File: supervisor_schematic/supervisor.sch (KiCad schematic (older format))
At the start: 13 parts

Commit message: supervisor almost done
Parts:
- added 10K: R6, symbol Device:R
- added C?: C1, symbol pspice:C
- added LS?: PS1240P02BT, PS1240P02BT, symbol Noggin:PS1240P02BT
- added R5: 1K, symbol Device:R
- added SW?: SW_Push, symbol Switch:SW_Push
- added U?: OLED-1602A, symbol Noggin:OLED-1602A
- D1: renamed from D?; value LED -> Green LED
- D2: renamed from D?; value LED -> Red LED
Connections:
- net +3V3: now also 10K.1, U?.~ (VSS)
- net GND: now also C?.2, LS?.2, U?.~ (VSS)
- net CS: now reaches ANT?.19 (CMD)
- net CS: now also U?.~ (VSS)
- net CLK: now reaches ANT?.20 (CLK)
- net CLK: now also U?.~ (VSS)
- net SD0: now reaches ANT?.21 (SD0)
- net SD0: now also U?.~ (VSS)
- net SD1: now reaches ANT?.22 (SD1)
- net SD1: now also U?.~ (VSS)
- net at ANT?.23 (IO15): now also R5.2
- net at ANT?.3 (EN): now also 10K.2, C?.1, SW?.1
- new net: LS?.1, R5.1
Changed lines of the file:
@@
 	4700 3000 4450 3000
 $Comp
-L Device:LED D?
+L Device:LED D1
 U 1 1 62152961
 P 4450 3400
-F 0 "D?" H 4443 3616 50  0000 C CNN
-F 1 "LED" H 4443 3525 50  0000 C CNN
+F 0 "D1" H 4443 3616 50  0000 C CNN
+F 1 "Green LED" H 4443 3525 50  0000 C CNN
 F 2 "" H 4450 3400 50  0001 C CNN
 F 3 "~" H 4450 3400 50  0001 C CNN
@@
 $EndComp
 $Comp
-L Device:LED D?
+L Device:LED D2
 U 1 1 62153081
 P 4000 3500
-F 0 "D?" H 3993 3716 50  0000 C CNN
-F 1 "LED" H 3993 3625 50  0000 C CNN
+F 0 "D2" H 3993 3716 50  0000 C CNN
+F 1 "Red LED" H 3993 3625 50  0000 C CNN
 F 2 "" H 4000 3500 50  0001 C CNN
 F 3 "~" H 4000 3500 50  0001 C CNN
@@
 Wire Wire Line
 	6450 5400 6300 5400
-Wire Wire Line
-	6450 5400 6600 5400
 Connection ~ 6450 5400
 $Comp
@@
 	1    0    0    -1
 $EndComp
+$Comp
+L Noggin:PS1240P02BT LS?
+U 1 1 6215B3F6
+P 6950 3100
+F 0 "LS?" H 7578 3096 50  0000 L CNN
+F 1 "PS1240P02BT" H 7578 3005 50  0000 L CNN
+F 2 "PS1240P02BT" H 7600 3200 50  0001 L CNN
+F 3 "https://product.tdk.com/system/files/dam/doc/product/sw_piezo/sw_piezo/piezo-buzzer/catalog/piezoelectronic_buzzer_ps_en.pdf" H 7600 3100 50  0001 L CNN
+F 4 "Piezoelectric Buzzers, Sound Pressure Level=70dB min, Freq.=4000Hz nom" H 7600 3000 50  0001 L CNN "Description"
+F 5 "TDK" H 7600 2800 50  0001 L CNN "Manufacturer_Name"
+F 6 "PS1240P02BT" H 7600 2700 50  0001 L CNN "Manufacturer_Part_Number"
+F 7 "810-PS1240P02BT" H 7600 2600 50  0001 L CNN "Mouser Part Number"
+F 8 "https://www.mouser.co.uk/ProductDetail/TDK/PS1240P02BT?qs=d7g9p1yFhWaZXSY9MjKMkw%3D%3D" H 7600 2500 50  0001 L CNN "Mouser Price/Stock"
+F 9 "PS1240P02BT" H 7600 2400 50  0001 L CNN "Arrow Part Number"
+F 10 "https://www.arrow.com/en/products/ps1240p02bt/tdk?region=nac" H 7600 2300 50  0001 L CNN "Arrow Price/Stock"
+	1    6950 3100
+	1    0    0    -1
+$EndComp
+$Comp
+L Device:R R5
+U 1 1 6215ED9A
+P 6500 3100
+F 0 "R5" V 6293 3100 50  0000 C CNN
+F 1 "1K" V 6384 3100 50  0000 C CNN
+F 2 "" V 6430 3100 50  0001 C CNN
+F 3 "~" H 6500 3100 50  0001 C CNN
+	1    6500 3100
+	0    1    1    0
+$EndComp
+Wire Wire Line
+	6100 3100 6350 3100
+Wire Wire Line
+	6650 3100 6950 3100
+Wire Wire Line
+	6450 5400 6600 5400
+Wire Wire Line
+	6950 3200 6950 5700
+Wire Wire Line
+	6950 6250 6600 6250
+$Comp
+L Noggin:OLED-1602A U?
+U 1 1 6216BA63
+P 9300 4000
+F 0 "U?" V 9124 4328 50  0000 L CNN
+F 1 "OLED-1602A" V 9215 4328 50  0000 L CNN
+F 2 "" H 9250 4100 50  0001 C CNN
+F 3 "" H 9250 4100 50  0001 C CNN
+	1    9300 4000
+	0    1    1    0
+$EndComp
+$Comp
+L power:+3.3V #PWR?
+U 1 1 6217008E
+P 8950 2950
+F 0 "#PWR?" H 8950 2800 50  0001 C CNN
+F 1 "+3.3V" V 8965 3078 50  0000 L CNN
+F 2 "" H 8950 2950 50  0001 C CNN
+F 3 "" H 8950 2950 50  0001 C CNN
+	1    8950 2950
+	0    -1   -1   0
+$EndComp
+Wire Wire Line
+	8200 5700 6950 5700
+Connection ~ 6950 5700
+Wire Wire Line
+	6950 5700 6950 6250
+Wire Wire Line
+	8200 3000 8200 5700
+Wire Wire Line
+	8200 3000 8950 3000
+Text GLabel 4700 4800 0    50   Input ~ 0
+CLK
+Text GLabel 8950 3650 0    50   Input ~ 0
+CLK
+Text GLabel 8650 3700 0    50   Input ~ 0
+SD1
+Text GLabel 8950 3750 0    50   Input ~ 0
+SD0
+Wire Wire Line
+	8950 3700 8650 3700
+Text GLabel 6100 3000 2    50   Input ~ 0
+SD1
+Text GLabel 6100 2900 2    50   Input ~ 0
+SD0
+Text GLabel 4700 4700 0    50   Input ~ 0
+CS
+Text GLabel 8950 3850 0    50   Input ~ 0
+CS
+$Comp
+L Device:R 10K
+U 1 1 6217785D
+P 2400 3000
+F 0 "10K" H 2470 3046 50  0000 L CNN
+F 1 "R6" H 2470 2955 50  0000 L CNN
+F 2 "" V 2330 3000 50  0001 C CNN
+F 3 "~" H 2400 3000 50  0001 C CNN
+	1    2400 3000
+	1    0    0    -1
+$EndComp
+$Comp
+L Switch:SW_Push SW?
+U 1 1 62178830
+P 2750 3500
+F 0 "SW?" V 2704 3648 50  0000 L CNN
+F 1 "SW_Push" V 2795 3648 50  0000 L CNN
+F 2 "" H 2750 3700 50  0001 C CNN
+F 3 "~" H 2750 3700 50  0001 C CNN
+	1    2750 3500
+	0    1    1    0
+$EndComp
+$Comp
+L pspice:C C?
+U 1 1 6217C01A
+P 2050 3550
+F 0 "C?" H 2228 3596 50  0000 L CNN
+F 1 "C1" H 2228 3505 50  0000 L CNN
+F 2 "" H 2050 3550 50  0001 C CNN
+F 3 "~" H 2050 3550 50  0001 C CNN
+	1    2050 3550
+	1    0    0    -1
+$EndComp
+$Comp
+L power:GND #PWR?
+U 1 1 6217CF2E
+P 2450 3900
+F 0 "#PWR?" H 2450 3650 50  0001 C CNN
+F 1 "GND" H 2455 3727 50  0000 C CNN
+F 2 "" H 2450 3900 50  0001 C CNN
+F 3 "" H 2450 3900 50  0001 C CNN
+	1    2450 3900
+	1    0    0    -1
+$EndComp
+$Comp
+L power:+3.3V #PWR?
+U 1 1 6217D564
+P 2400 2850
+F 0 "#PWR?" H 2400 2700 50  0001 C CNN
+F 1 "+3.3V" H 2415 3023 50  0000 C CNN
+F 2 "" H 2400 2850 50  0001 C CNN
+F 3 "" H 2400 2850 50  0001 C CNN
+	1    2400 2850
+	1    0    0    -1
+$EndComp
+Wire Wire Line
+	2750 3750 2750 3900
+Wire Wire Line
+	2750 3900 2450 3900
+Wire Wire Line
+	2750 3300 2750 3150
+Wire Wire Line
+	2750 3150 2400 3150
+Wire Wire Line
+	2050 3300 2050 3150
+Wire Wire Line
+	2050 3150 2400 3150
+Connection ~ 2400 3150
+Wire Wire Line
+	2050 3800 2050 3900
+Wire Wire Line
+	2050 3900 2450 3900
+Connection ~ 2450 3900
+Wire Wire Line
+	2750 3150 2750 3100
+Wire Wire Line
+	2750 3100 4700 3100
+Connection ~ 2750 3150
 $EndSCHEMATC

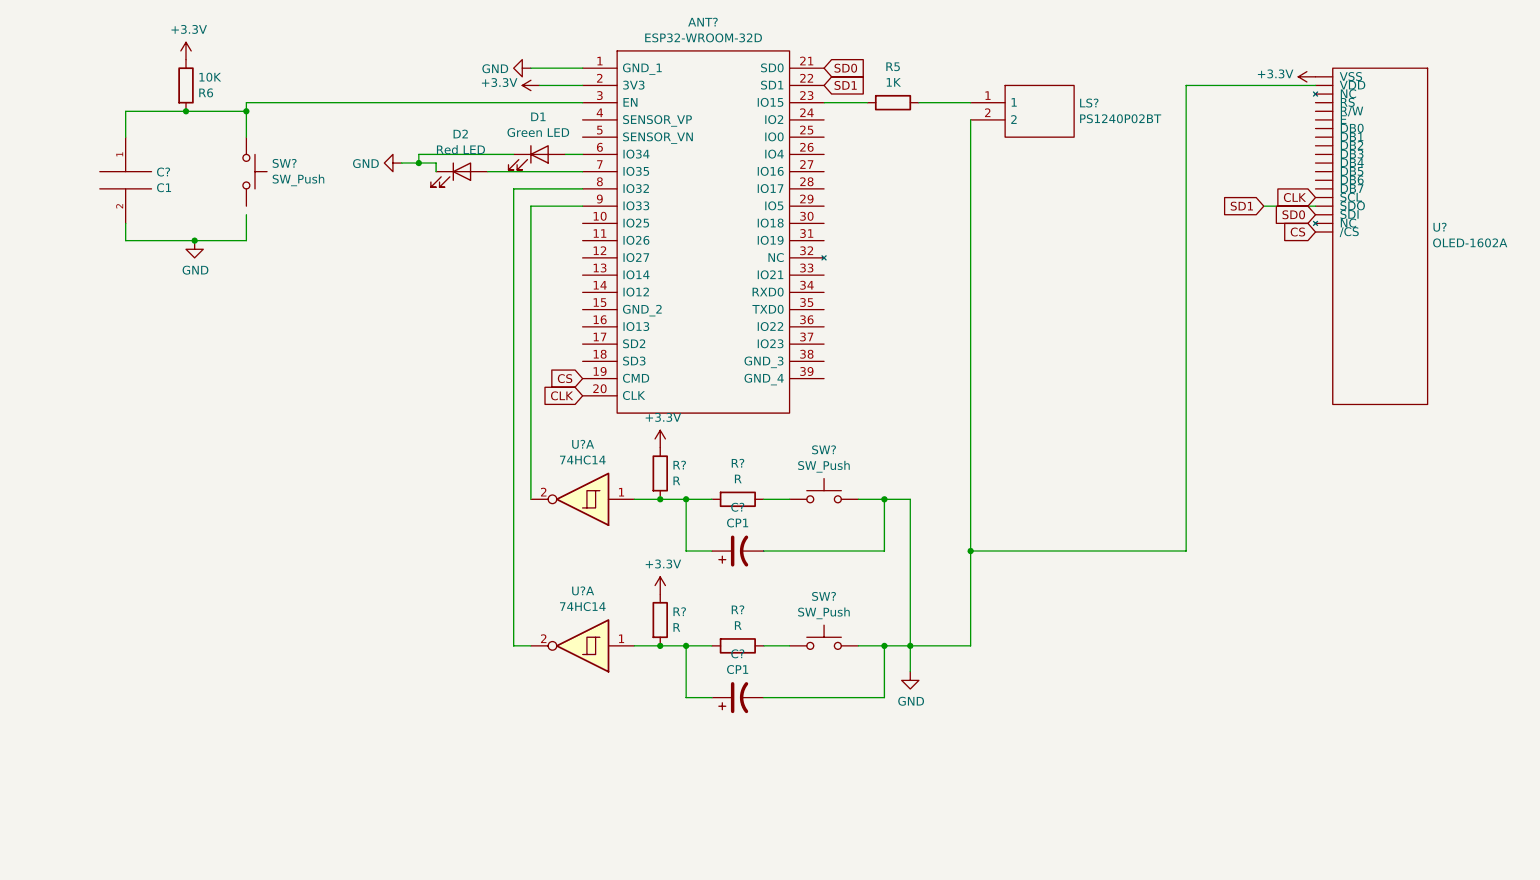
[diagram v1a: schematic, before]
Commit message: button debouncing schem
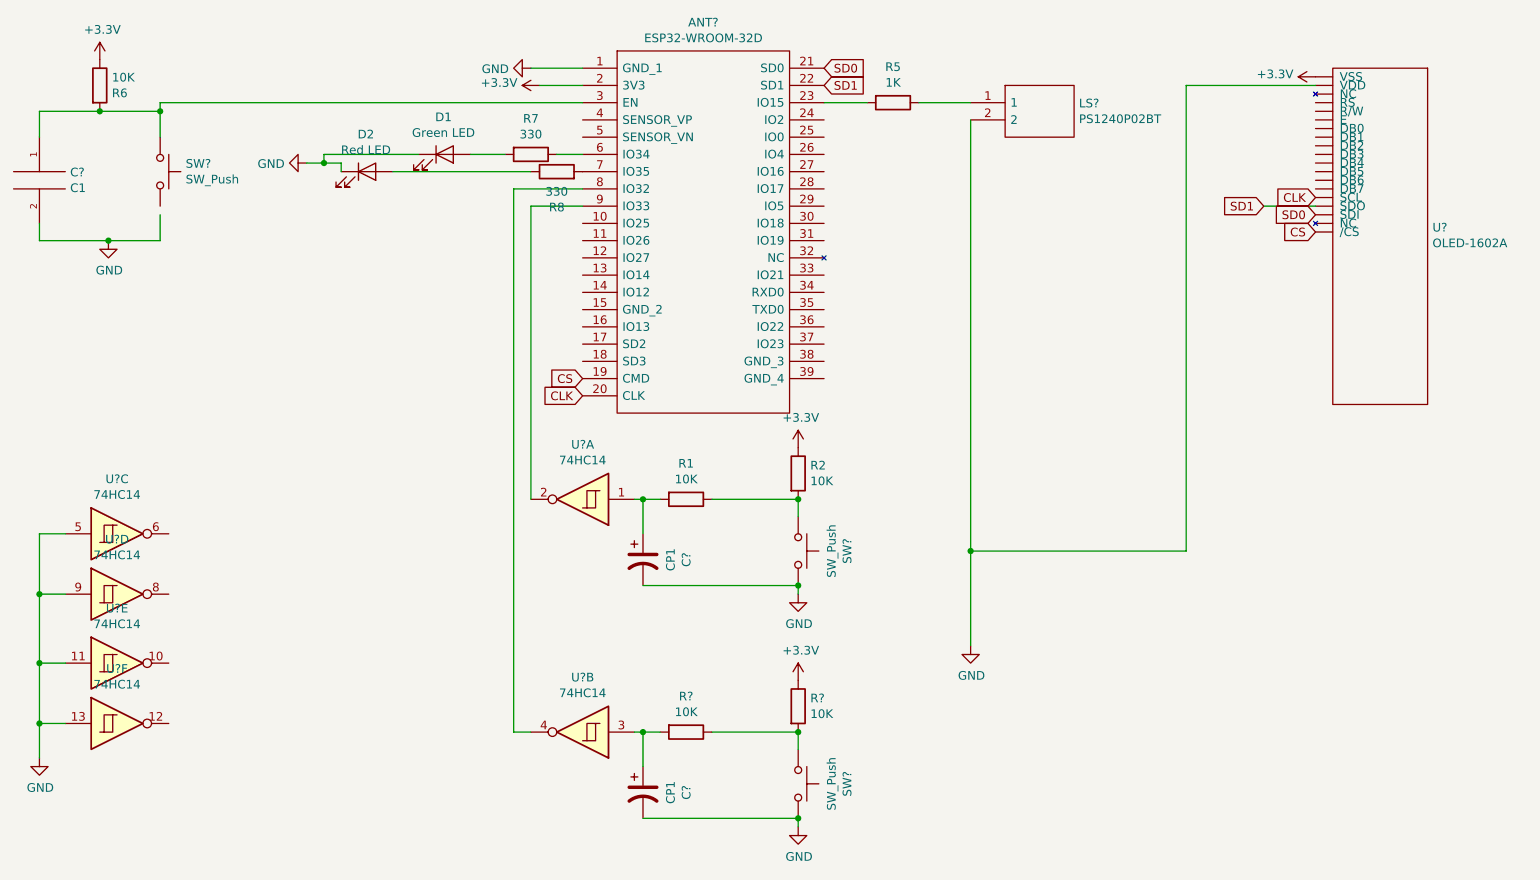
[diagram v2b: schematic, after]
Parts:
- removed C?: CP1, symbol Device:CP1
- removed R? (x2): R, symbol Device:R
- removed SW?: SW_Push, symbol Switch:SW_Push
- removed U?: 74HC14, symbol 74xx:74HC14
- added C?: CP1, symbol Device:CP1
- added R7, R8: 330, symbol Device:R
- added R? (x2): 10K, symbol Device:R
- added SW?: SW_Push, symbol Switch:SW_Push
- added U? (x5): 74HC14, symbol 74xx:74HC14
- R1, R2: renamed from R?; value R -> 10K
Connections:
- net +3V3: now also R?.1
- net GND: now also C?.2, SW?.2, U?.11, U?.13, U?.5, U?.9
- net at ANT?.6 (IO34): now also R7.1; no longer D1.2 (A)
- net at ANT?.7 (IO35): now also R8.2; no longer D2.2 (A)
- net at ANT?.8 (IO32): now also U?.4
- net at C?.1, R1.2, U?.1: no longer R2.2
- net at R1.1, SW?.1: now also R2.2
- new net: D1.2 (A), R7.2
- new net: D2.2 (A), R8.1
- new net: C?.1, R?.2, U?.3
- new net: R?.1, R?.2, SW?.1
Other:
- moved on the sheet: 10K, C?, D1, D2, R1, R2, SW?
